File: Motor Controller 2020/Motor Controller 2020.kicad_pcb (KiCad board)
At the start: 2 copper layers, 86 x 60 mm, 48 parts, among them J1 Batt+, J2 Batt-, J3 Input, J4 Motor+, J5 Motor-, Q1 IRF1404, Q2 IRF1404, Q3 IRF1404, Q4 IRF1404, Q5 IRF1404, Q6 IRF1404, Q7 IRF1404, Q8 IRF1404, SW1 SW_DIP_x03, U1 MAX15062A, U2 a4956, U3 Attiny4313

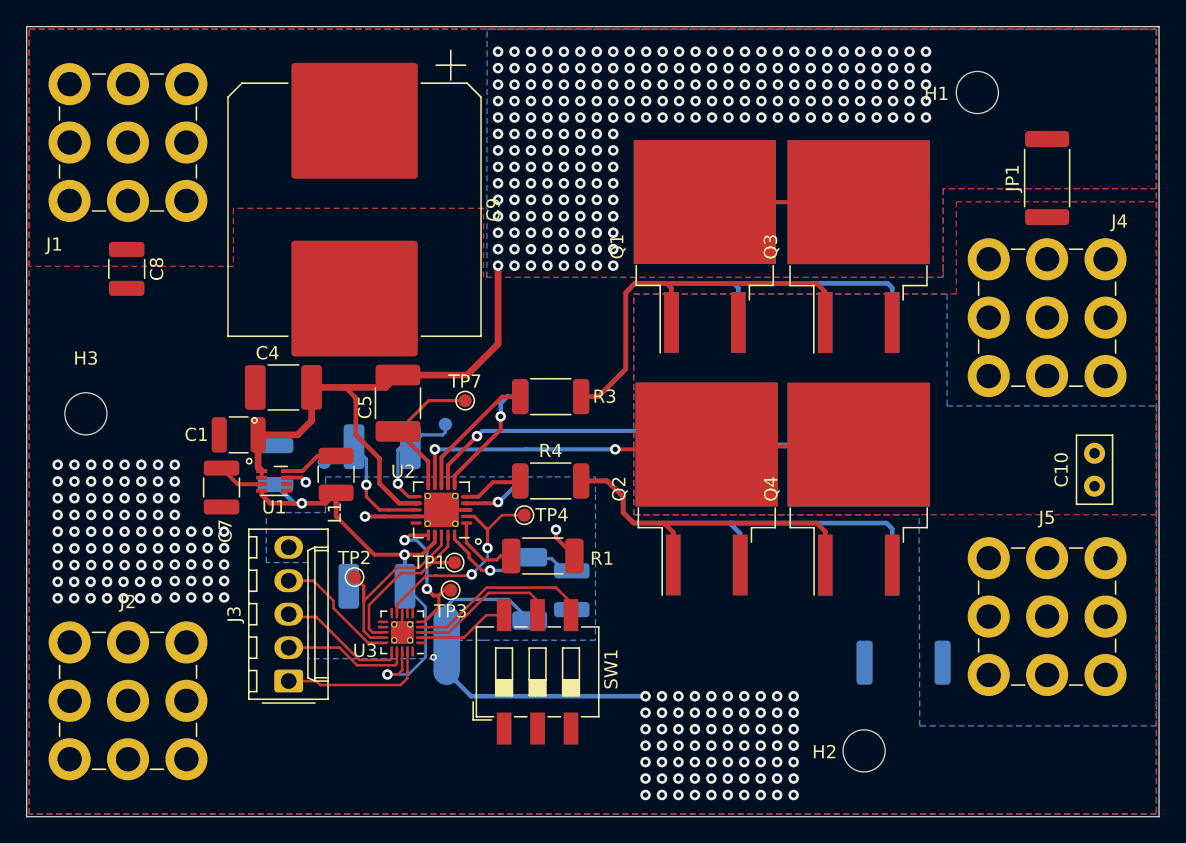
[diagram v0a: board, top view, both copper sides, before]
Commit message: Updated schematic and PCB
Reduced the loop length to just over half the original length. Added more Vias for stitching. Changed MOSFET to handle up to 48V, meaning that the system can work up to 48V while still maintaining the 65A continuous rating.
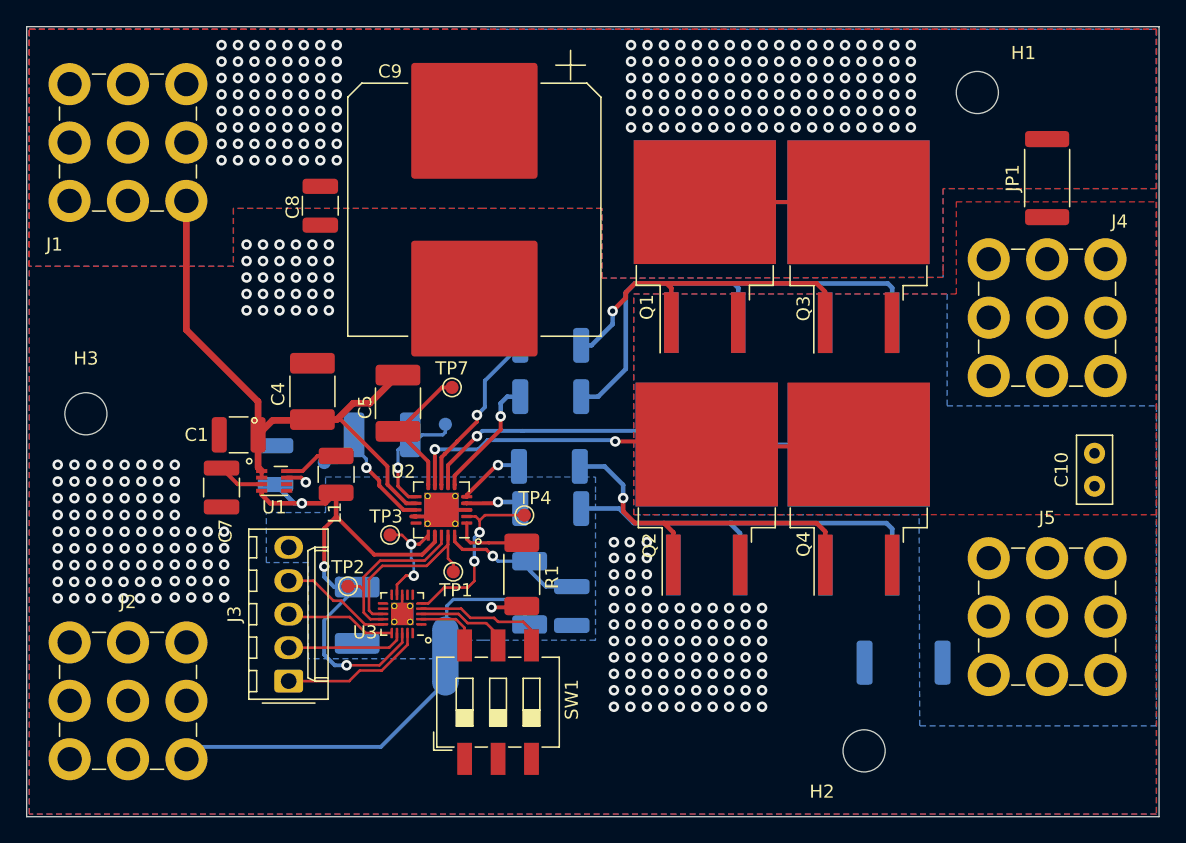
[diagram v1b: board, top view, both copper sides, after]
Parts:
- C8: value 10uF -> 1uF
- R3, R4: moved to B.Cu
- TP1: value TestPoint -> Direction
- TP2: value TestPoint -> PWM
- TP3: value TestPoint -> Fault
- TP4: value TestPoint -> Mode
- TP5: value TestPoint -> CP1
- TP6: value TestPoint -> CP2
- TP7: value TestPoint -> VCP
- moved C8 15.5 mm to (111.0, 56.5)
- moved C9 9.10 mm to (122.7, 56.8)
- moved TP3 6.23 mm to (116.3, 81.5)
- moved R3 3.90 mm to (128.5, 67.1)
- moved SW1 3.78 mm to (124.5, 94.2)
- moved C11 2.66 mm to (113.8, 87.6), turned to 90 degrees
- moved C4 2.22 mm to (110.4, 70.6), turned to 270 degrees
- moved R1 2.13 mm to (126.3, 84.5), turned to 90 degrees
- moved R6 2.10 mm to (128.5, 79.5)
- moved TP7 1.41 mm to (121.0, 70.3)
- moved U3 1.40 mm to (117.2, 87.5)
- moved C6 1.20 mm to (130.1, 86.9)
- moved R4 1.10 mm to (128.4, 76.3)
- moved C3 0.90 mm to (115.7, 73.9)
- moved TP2 0.86 mm to (113.1, 85.4)
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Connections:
- net +12V renamed VCC
- U3 pad 5: Fault -> Mode
- U3 pad 9: Mode -> Fault
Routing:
- net +5V: track 36.9 -> 44.4 mm
- net GND: track 17.5 -> 23.8 mm, vias 158 -> 200
- net MOTOR+: track 47.7 -> 41.7 mm
- net ADDR_Select_2: track 11.7 -> 7.29 mm
- net Net-(Q1-Pad1): track 33.1 -> 28.9 mm, vias 0 -> 1
- net Fault: track 11.5 -> 8.33 mm
- net GHA: track 10.2 -> 13.3 mm, vias 0 -> 1
- net GNDD: track 21.0 -> 18.1 mm, vias 2 -> 1
- net ADDR_Select_1: track 14.0 -> 11.8 mm
- net VCC: track 67.5 -> 69.7 mm, vias 207 -> 172
- net ADDR_Select_3: track 7.00 -> 4.90 mm
- net Mode: track 16.6 -> 14.6 mm
- net Net-(Q5-Pad1): track 40.0 -> 38.5 mm
- net MISO: track 9.84 -> 8.41 mm
- net PWM: track 14.5 -> 13.3 mm
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
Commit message: Re-arranged components
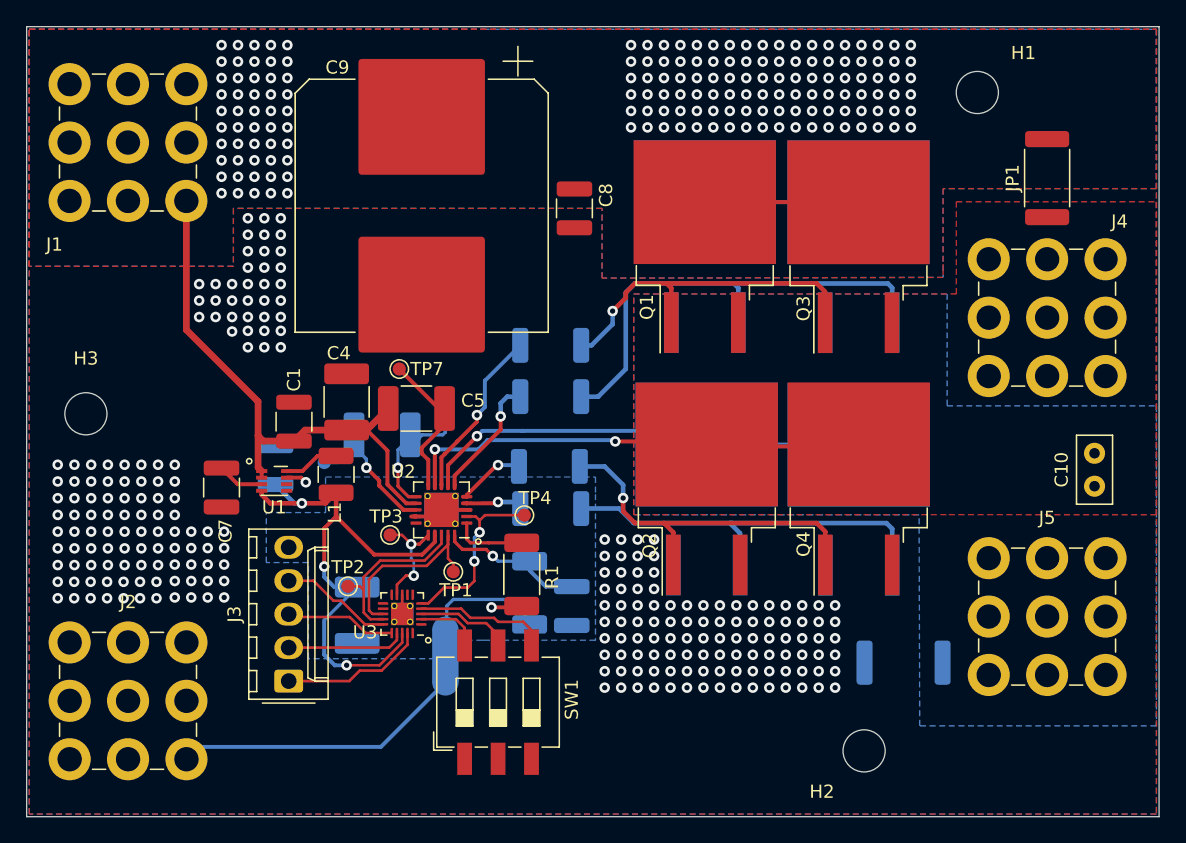
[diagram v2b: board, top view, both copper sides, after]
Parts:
- moved C8 19.3 mm to (130.3, 56.7)
- moved C1 4.32 mm to (109.0, 72.9), turned to 90 degrees
- moved TP7 4.24 mm to (117.0, 68.9)
- moved C9 4.01 mm to (118.7, 56.5)
- moved C4 2.72 mm to (113.0, 71.4)
- moved C5 1.46 mm to (118.3, 71.9), turned to 0 degrees
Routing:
- net VCC: track 69.7 -> 67.9 mm, vias 172 -> 158
- net Net-(C5-Pad2): track 10.7 -> 11.7 mm
- net GND: vias 200 -> 231

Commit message: Updated PCB
Added larger caps for local storage. Also removed 4 MOSFETS because I don't believe I will need them. This will be tested when the system works properly
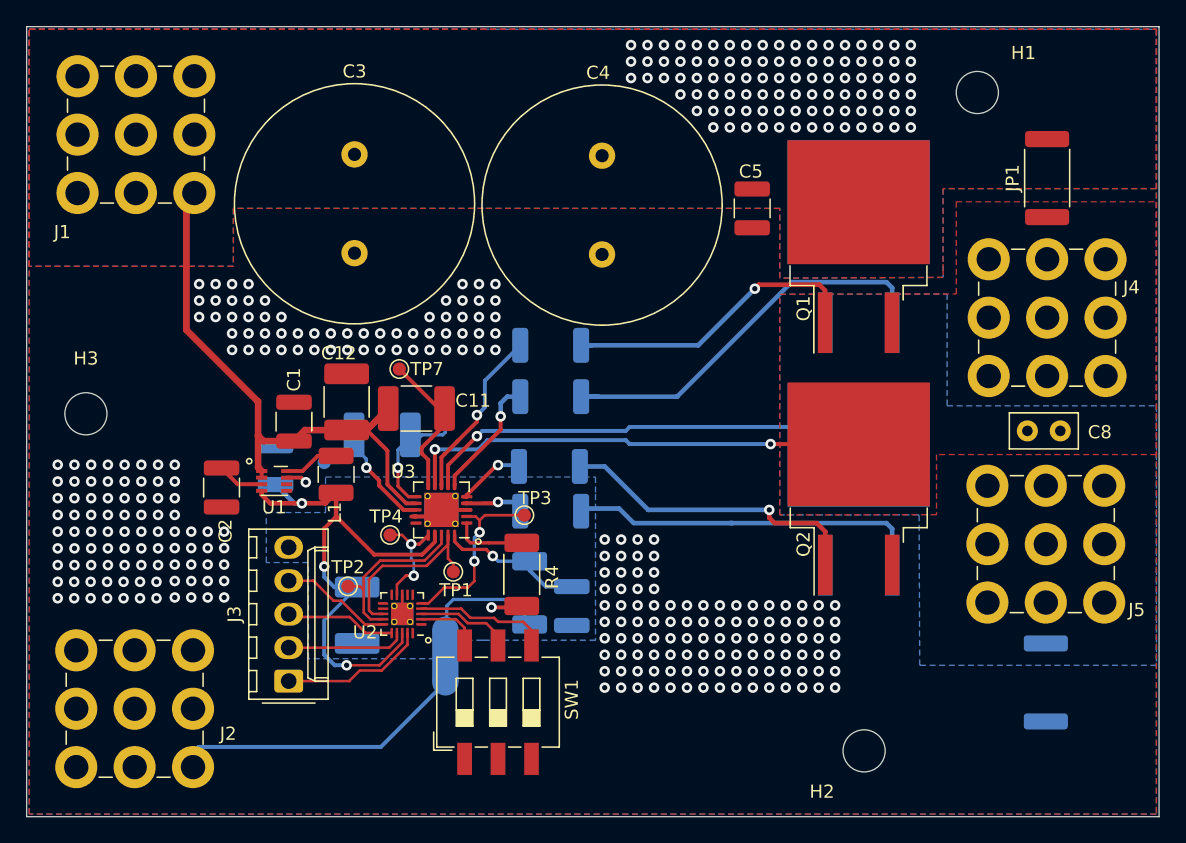
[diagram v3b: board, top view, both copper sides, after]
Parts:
- removed the C9 at (118.7, 56.5)
- removed the Q1 at (140.2, 59.6)
- removed the Q2 at (140.4, 78.0)
- removed Q6, Q8: IRF1404, Package_TO_SOT_SMD:TO-263-2
- removed the R4 at (128.4, 76.3)
- added C3: 2200uF, Capacitor_THT:C_Radial_D18.0mm_H35.5mm_P7.50mm, F.Cu at (113.6, 52.6)
- added C4: 2200uF, Capacitor_THT:C_Radial_D18.0mm_H35.5mm_P7.50mm, F.Cu at (132.4, 52.7)
- added R2: 100, Resistor_SMD:R_2010_5025Metric, B.Cu at (128.4, 76.3)
- C11: renamed from C5; value 0.47uF -> 0.1uF
- moved C5 13.5 mm to (143.8, 56.7)
- moved JP2 10.9 mm to (166.1, 92.7), turned to 270 degrees
- moved J5 5.50 mm to (166.1, 82.2)
- moved C8 4.94 mm to (167.2, 73.6), turned to 180 degrees
- moved J1 0.85 mm to (97.0, 51.1)
- moved J2 0.78 mm to (96.9, 94.7)
- moved R6 0.20 mm to (128.5, 79.7)
- renumbered C3 to C10, C4 to C12, C7 to C2, C8 to C5, C2 to C6, C11 to C7, C10 to C8, C6 to C9, Q3 to Q1, Q4 to Q2, Q7 to Q3, Q5 to Q4, R3 to R1, R2 to R3, R1 to R4, TP4 to TP3, TP3 to TP4, U3 to U2, U2 to U3
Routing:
- net VCC: track 67.9 -> 44.7 mm, vias 158 -> 96
- net Net-(Q1-Pad1): track 28.9 -> 23.7 mm
- net Net-(Q3-Pad1): track 36.5 -> 31.3 mm
- net Net-(Q2-Pad1): track 28.0 -> 23.7 mm
- net Net-(Q4-Pad1): track 38.5 -> 34.9 mm
- net MOTOR+: track 41.7 -> 38.4 mm
- net MOTOR-: track 37.7 -> 35.2 mm
- net GND: vias 231 -> 255

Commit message: Add files via upload
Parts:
- moved Q4 5.42 mm to (148.5, 73.8), turned to 0 degrees
- moved Q2 5.40 mm to (148.5, 73.8), turned to 0 degrees
- moved R4 2.62 mm to (128.3, 82.8), turned to 180 degrees
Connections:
- C9 pad 2: GNDD -> GND
- R3 pad 1: GNDD -> GND
- R4 pad 1: GNDD -> GND
- U3 pad 14: GNDD -> GND
- U3 pad 21: GNDD -> GND
- U3 pad 3: GNDD -> GND
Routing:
- net Net-(Q4-Pad1): track 34.9 -> 13.3 mm
- net GNDD: track 18.1 -> 2.59 mm, vias 1 -> 0
- net Net-(Q2-Pad1): track 23.7 -> 16.0 mm
- net GND: track 23.8 -> 28.8 mm, vias 255 -> 239
- net MOTOR-: track 35.2 -> 37.0 mm
- net Net-(Q3-Pad1): track 31.3 -> 32.9 mm
- net Net-(Q1-Pad1): track 23.7 -> 24.3 mm

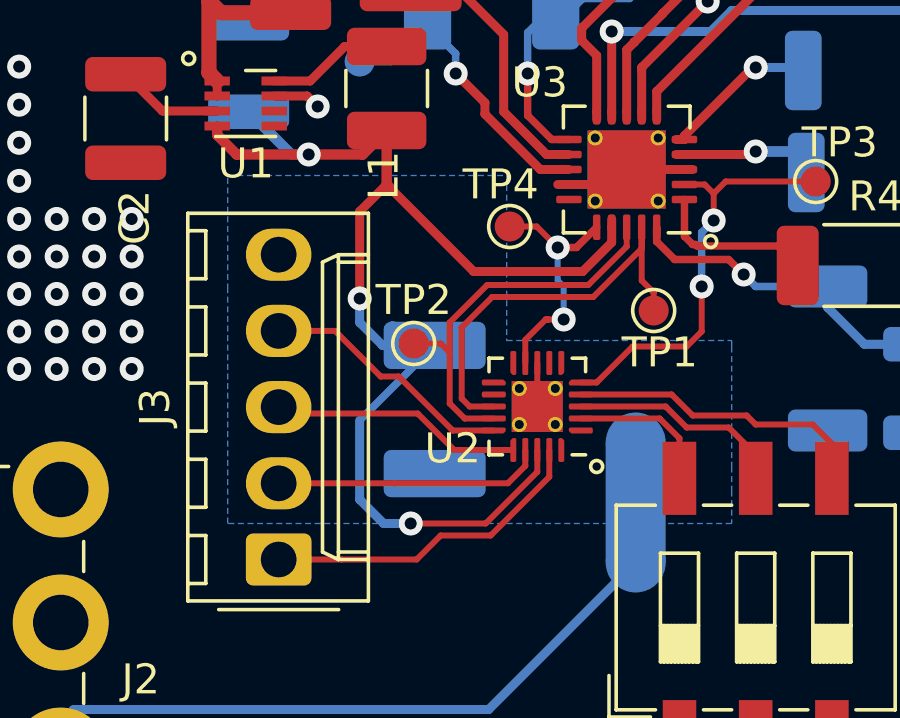
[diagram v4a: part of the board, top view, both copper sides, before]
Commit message: Remade and checked gerber files
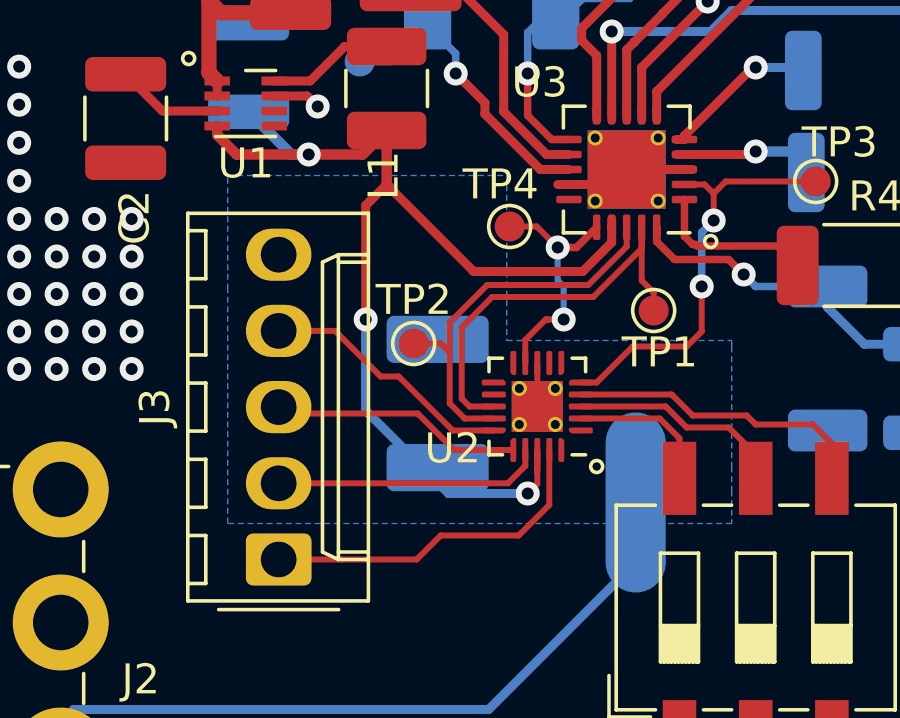
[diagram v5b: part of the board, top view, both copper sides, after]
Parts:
- moved C7 0.22 mm to (113.9, 87.4), turned to 270 degrees
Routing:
- net +5V: track 44.4 -> 37.8 mm
- net GNDD: track 2.59 -> 4.27 mm
- net A_RESET: track 11.1 -> 11.6 mm

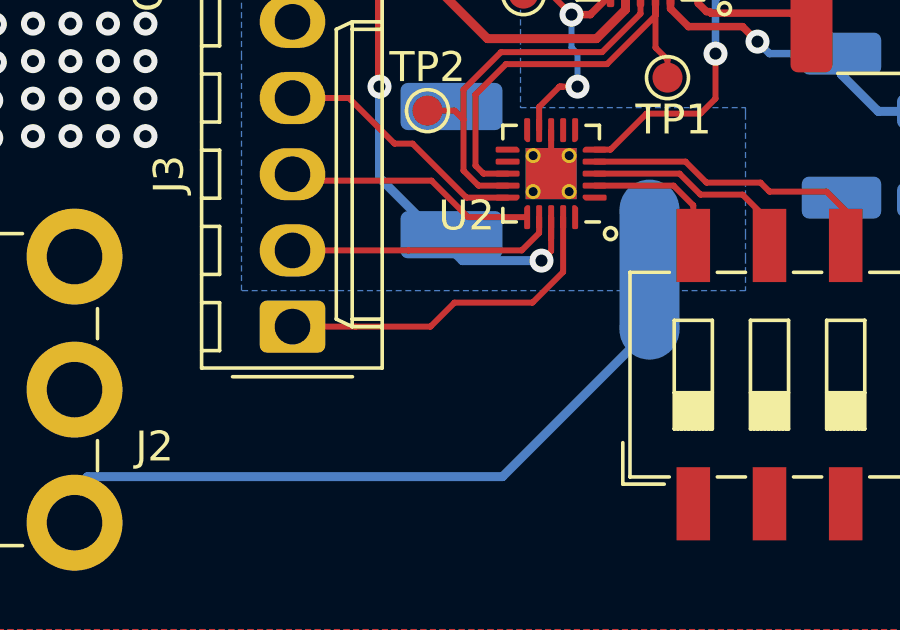
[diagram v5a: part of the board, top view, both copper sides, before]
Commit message: Added status lights
Added power and status lights to help diagnose issues when the system is running without screen on the master controller
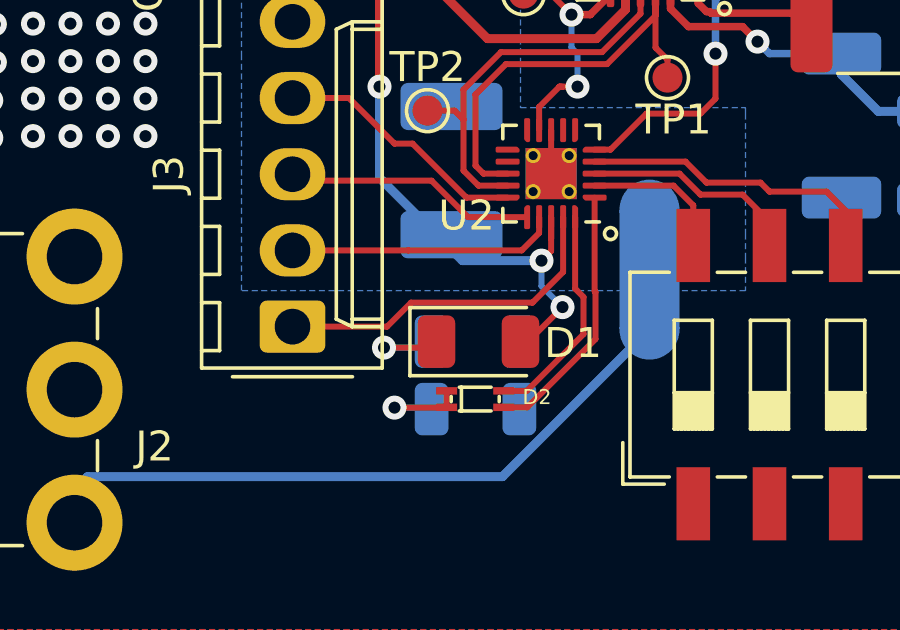
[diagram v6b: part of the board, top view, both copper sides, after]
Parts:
- added D1: Power On, LED_SMD:LED_1206_3216Metric, F.Cu at (114.8, 93.1)
- added D2: Status LED, Motor Controller 2020:LED_0603_4_pin, F.Cu at (114.8, 94.0)
- added R7: 150, Resistor_SMD:R_1206_3216Metric, B.Cu at (114.7, 93.1)
- added R8: 150, Resistor_SMD:R_1206_3216Metric, B.Cu at (114.7, 95.3)
- C6: value 10uF -> 22uF
- L1: value 47uH -> 68uH
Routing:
- net Net-(D2-Pad4): track 0.00 -> 8.73 mm
- net Net-(D2-Pad2): track 0.00 -> 7.46 mm
- net Net-(D1-Pad1): track 0.00 -> 3.74 mm, vias 0 -> 1
- net +5V: track 37.8 -> 41.5 mm, vias 3 -> 4
- net Net-(D2-Pad1): track 0.00 -> 3.55 mm, vias 0 -> 1
